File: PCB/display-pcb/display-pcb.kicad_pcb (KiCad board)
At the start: 2 copper layers, 128 x 57 mm, 7 parts, among them J1 B6B-XH-A, J2 B8B-XH-A, SW1 PTS645SL50-2 LFS, SW2 PTS645SL50-2 LFS, SW3 PTS645SL50-2 LFS, SW4 PTS645SL50-2 LFS, U1 NHD-C12864A1Z

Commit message: changes to display and tube pcb
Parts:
- J1, J2: moved to B.Cu
- moved J2 35.7 mm to (122.5, 61.0)
- moved J1 0.25 mm to (122.5, 30.5)
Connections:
- net Net-(U1-SCL) renamed SCL
- net Net-(U1-/RESET) renamed /RESET
- J1 pad 1: Net-(J1-Pad1) -> GND
- J1 pad 2: Net-(J1-Pad2) -> BTN0
- J1 pad 3: Net-(J1-Pad3) -> BTN1
- J1 pad 4: Net-(J1-Pad4) -> BTN2
- J1 pad 5: unconnected-(J1-Pad5) -> BTN3
- J2 pad 2: unconnected-(J2-Pad2) -> GND
- J2 pad 4: Net-(U1-SI) -> GND
- J2 pad 5: Net-(U1-A0) -> SI
- J2 pad 7: Net-(U1-/CS) -> A0
- J2 pad 8: GND -> /CS
- SW1 pad 1: Net-(J1-Pad1) -> BTN0
- SW2 pad 1: Net-(J1-Pad2) -> BTN1
- SW3 pad 1: Net-(J1-Pad3) -> BTN2
- SW4 pad 1: Net-(J1-Pad4) -> BTN3
- U1 pad 3: Net-(U1-SI) -> SI
- U1 pad 5: Net-(U1-A0) -> A0
- U1 pad 7: Net-(U1-/CS) -> /CS
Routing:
- net A0: track 0.00 -> 72.8 mm
- net /CS: track 0.00 -> 68.1 mm
- net SI: track 0.00 -> 60.0 mm
- net 3V3: track 86.1 -> 125.5 mm
- net /RESET: track 31.6 -> 67.0 mm
- net SCL: track 23.2 -> 58.6 mm
- net Net-(U1-/CS): track 33.4 -> 0.00 mm
- net Net-(J1-Pad2): track 31.4 -> 0.00 mm
- net Net-(U1-SI): track 31.3 -> 0.00 mm
- net BTN1: track 0.00 -> 30.5 mm
- net Net-(U1-A0): track 29.8 -> 0.00 mm
- net Net-(J1-Pad4): track 22.6 -> 0.00 mm
- net BTN3: track 0.00 -> 21.6 mm
- net BTN0: track 0.00 -> 19.8 mm
- net Net-(J1-Pad1): track 19.1 -> 0.00 mm
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
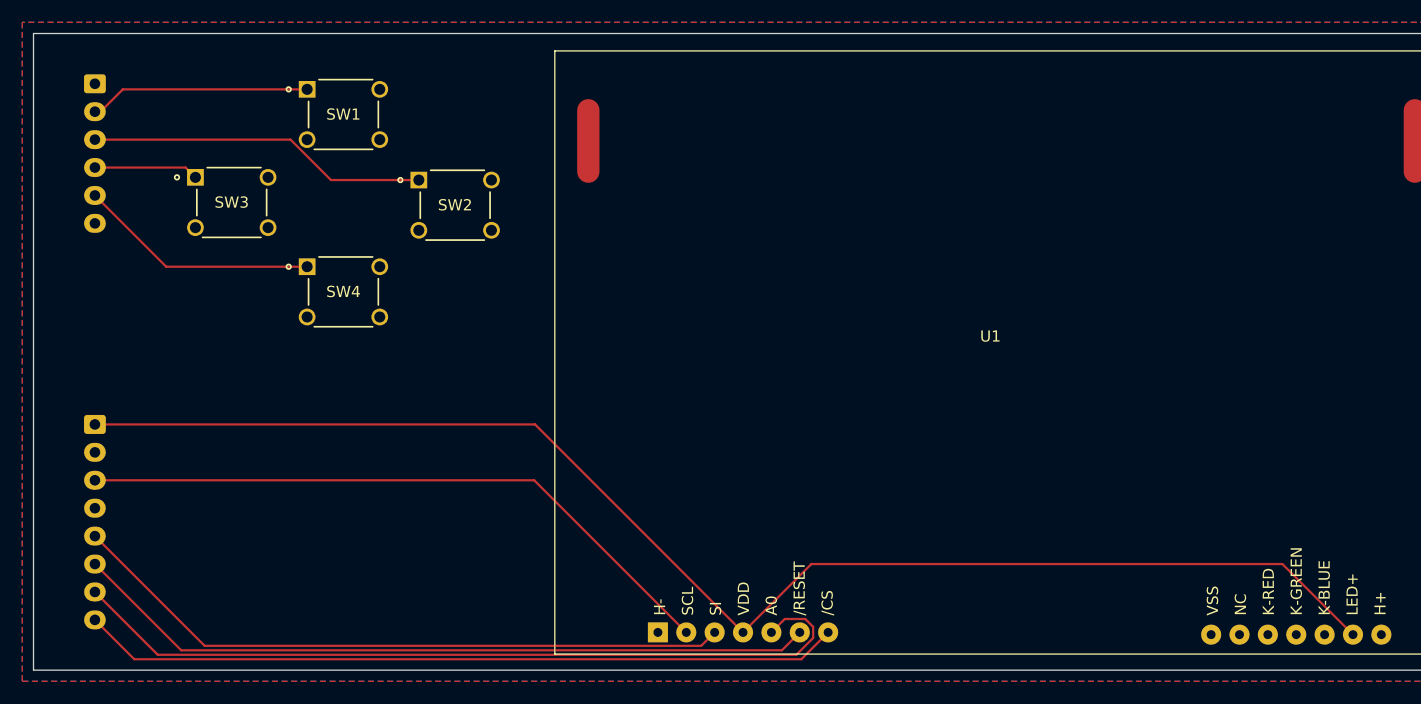
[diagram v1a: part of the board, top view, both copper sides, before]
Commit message: pcb silkscreens mostly
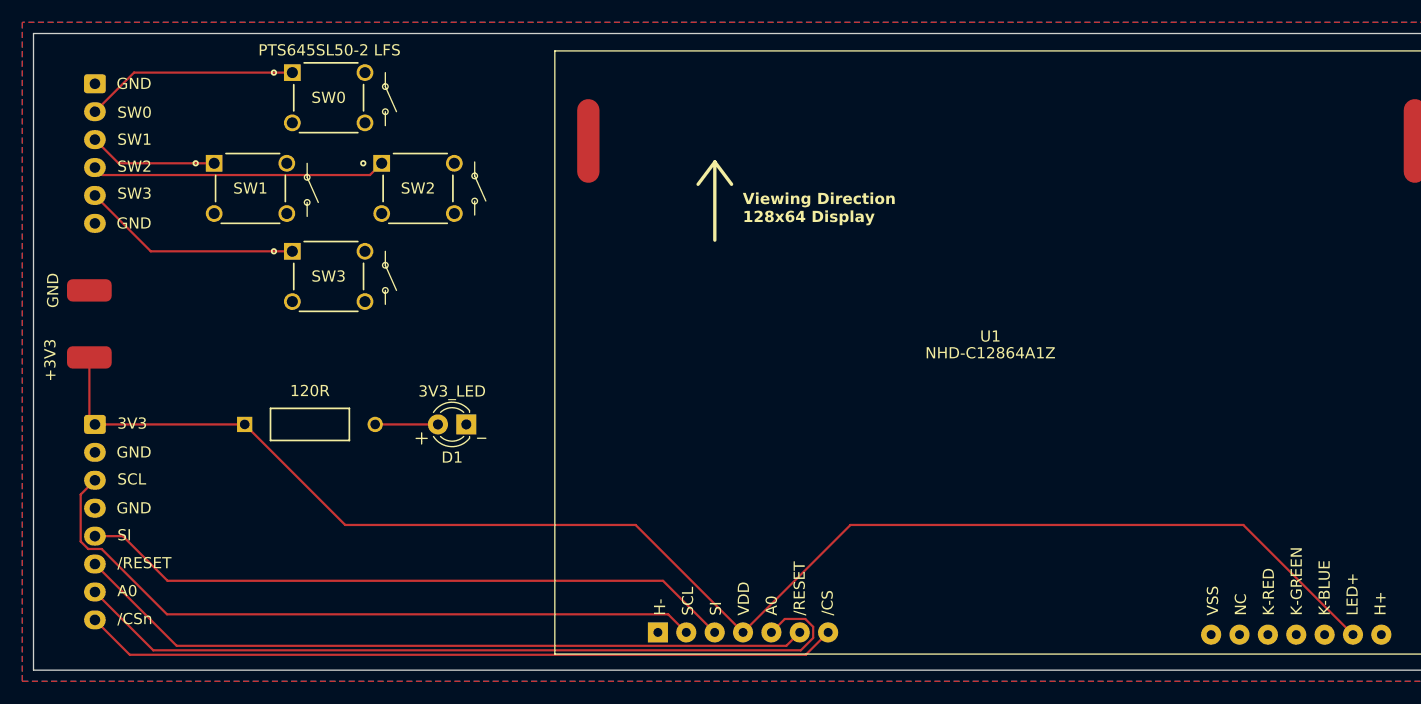
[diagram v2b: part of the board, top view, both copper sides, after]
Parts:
- removed SW4: PTS645SL50-2 LFS, footprints:PTS654S_CNK
- added +3V3: 3V3_Pad, Connector_Wire:SolderWirePad_1x01_SMD_2x4mm, F.Cu at (122.0, 55.0)
- added 120R: 120R, 10k-resistor:YAG_MF25_YAG, F.Cu at (135.9, 61.0)
- added D1: 3V3_LED, LED_THT:LED_D3.0mm, F.Cu at (155.8, 61.0)
- added GND: GND_Pad, Connector_Wire:SolderWirePad_1x01_SMD_2x4mm, F.Cu at (122.0, 49.0)
- added SW0: PTS645SL50-2 LFS, footprints:PTS654S_CNK, F.Cu at (140.2, 29.5)
- moved SW3 10.9 mm to (140.2, 45.5)
- moved SW1 10.6 mm to (133.2, 37.6)
- moved SW2 3.65 mm to (148.2, 37.6)
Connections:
- SW1 pad 1: BTN0 -> BTN1
- SW2 pad 1: BTN1 -> BTN2
- SW3 pad 1: BTN2 -> BTN3
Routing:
- net BTN1: track 30.5 -> 11.6 mm
- net BTN2: track 9.36 -> 26.4 mm
- net 3V3: track 125.5 -> 134.6 mm
- net Net-(D1-A): track 0.00 -> 5.62 mm
- net SCL: track 58.6 -> 63.6 mm
- net BTN3: track 21.6 -> 19.7 mm
- net SI: track 60.0 -> 59.1 mm
- net BTN0: track 19.8 -> 19.1 mm
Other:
- board text added: "/CSn"
- board text added: "/RESET"
- board text added: "3V3"
- board text added: "A0"
- board text added: "GND"
- board text added: "SCL"
- board text added: "SI"
- board text added: "SW0"
- board text added: "SW1"
- board text added: "SW2"
- board text added: "SW3"
- board text added: "Viewing Direction 128x64 Display"

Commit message: pcb stuff i forget
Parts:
- removed +3V3: 3V3_Pad, Connector_Wire:SolderWirePad_1x01_SMD_2x4mm
- removed GND: GND_Pad, Connector_Wire:SolderWirePad_1x01_SMD_2x4mm
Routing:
- net 3V3: track 134.6 -> 129.1 mm
- removed copper zone on F.Cu, net GND
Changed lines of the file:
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@@
 			(outputformat 1)
 			(mirror no)
-			(drillshape 1)
+			(drillshape 0)
 			(scaleselection 1)
-			(outputdirectory "")
+			(outputdirectory "gerber/")
 		)
 	)
@@
 		)
 	)
-	(footprint "Connector_Wire:SolderWirePad_1x01_SMD_2x4mm"
-		(layer "F.Cu")
-		(at 122 49 90)
-		(descr "Wire Pad, Square, SMD Pad,  2mm x 4mm")
-		(tags "MeasurementPoint Square SMDPad 2mmx4mm ")
-		(property "Reference" "GND"
-			(at 0 -3.25 270)
-			(layer "F.SilkS")
-			(effects
-				(font
-					(size 1 1)
-					(thickness 0.15)
-				)
-			)
-		)
-		(property "Value" "GND_Pad"
-			(at 0 2.54 90)
-			(layer "F.Fab")
-			(effects
-				(font
-					(size 1 1)
-					(thickness 0.15)
-				)
-			)
-		)
-		(property "Datasheet" "~"
-			(at 0 0 90)
-			(layer "F.Fab")
-			(hide yes)
-			(effects
-				(font
-					(size 1.27 1.27)
-					(thickness 0.15)
-				)
-			)
-		)
-		(property "Description" "Generic connector, single row, 01x01, script generated"
-			(at 0 0 90)
-			(layer "F.Fab")
-			(hide yes)
-			(effects
-				(font
-					(size 1.27 1.27)
-					(thickness 0.15)
-				)
-			)
-		)
-		(property ki_fp_filters "Connector*:*_1x??_*")
-		(sheetname "/")
-		(sheetfile "display-pcb.kicad_sch")
-		(attr exclude_from_pos_files)
-		(fp_rect
-			(start -1.25 -2.25)
-			(end 1.25 2.25)
-			(stroke
-				(width 0.05)
-				(type solid)
-			)
-			(fill no)
-			(layer "F.CrtYd")
-		)
-		(fp_rect
-			(start -1.15 -2.15)
-			(end 1.15 2.15)
-			(stroke
-				(width 0.1)
-				(type default)
-			)
-			(fill no)
-			(layer "F.Fab")
-		)
-		(fp_text user "${REFERENCE}"
-			(at 0 0 90)
-			(layer "F.Fab")
-			(effects
-				(font
-					(size 1 1)
-					(thickness 0.15)
-				)
-			)
-		)
-		(pad "1" smd roundrect
-			(at 0 0 90)
-			(size 2 4)
-			(layers "F.Cu" "F.Mask")
-			(roundrect_rratio 0.25)
-			(net 4 "GND")
-			(pinfunction "Pin_1")
-			(pintype "passive")
-		)
-		(embedded_fonts no)
-	)
 	(footprint "footprints:PTS654S_CNK"
 		(layer "F.Cu")
@@
 		(embedded_fonts no)
 	)
-	(footprint "Connector_Wire:SolderWirePad_1x01_SMD_2x4mm"
-		(layer "F.Cu")
-		(at 122 55 90)
-		(descr "Wire Pad, Square, SMD Pad,  2mm x 4mm")
-		(tags "MeasurementPoint Square SMDPad 2mmx4mm ")
-		(property "Reference" "+3V3"
-			(at -0.25 -3.5 270)
-			(layer "F.SilkS")
-			(effects
-				(font
-					(size 1 1)
-					(thickness 0.15)
-				)
-			)
-		)
-		(property "Value" "3V3_Pad"
-			(at 0 2.54 90)
-			(layer "F.Fab")
-			(effects
-				(font
-					(size 1 1)
-					(thickness 0.15)
-				)
-			)
-		)
-		(property "Datasheet" "~"
-			(at 0 0 90)
-			(layer "F.Fab")
-			(hide yes)
-			(effects
-				(font
-					(size 1.27 1.27)
-					(thickness 0.15)
-				)
-			)
-		)
-		(property "Description" "Generic connector, single row, 01x01, script generated"
-			(at 0 0 90)
-			(layer "F.Fab")
-			(hide yes)
-			(effects
-				(font
-					(size 1.27 1.27)
-					(thickness 0.15)
-				)
-			)
-		)
-		(property ki_fp_filters "Connector*:*_1x??_*")
-		(sheetname "/")
-		(sheetfile "display-pcb.kicad_sch")
-		(attr exclude_from_pos_files)
-		(fp_rect
-			(start -1.25 -2.25)
-			(end 1.25 2.25)
-			(stroke
-				(width 0.05)
-				(type solid)
-			)
-			(fill no)
-			(layer "F.CrtYd")
-		)
-		(fp_rect
-			(start -1.15 -2.15)
-			(end 1.15 2.15)
-			(stroke
-				(width 0.1)
-				(type default)
-			)
-			(fill no)
-			(layer "F.Fab")
-		)
-		(fp_text user "${REFERENCE}"
-			(at 0 0 90)
-			(layer "F.Fab")
-			(effects
-				(font
-					(size 1 1)
-					(thickness 0.15)
-				)
-			)
-		)
-		(pad "1" smd roundrect
-			(at 0 0 90)
-			(size 2 4)
-			(layers "F.Cu" "F.Mask")
-			(roundrect_rratio 0.25)
-			(net 8 "3V3")
-			(pinfunction "Pin_1")
-			(pintype "passive")
-		)
-		(embedded_fonts no)
-	)
 	(footprint "footprints:PTS654S_CNK"
 		(layer "F.Cu")
@@
 	)
 	(segment
-		(start 122 55)
-		(end 122 60.5)
-		(width 0.2)
-		(layer "F.Cu")
-		(net 8)
-	)
-	(segment
 		(start 180.52425 79.61995)
 		(end 190.1442 70)
@@
 		(net_name "GND")
 		(locked yes)
-		(layers "F.Cu" "B.Cu")
+		(layer "B.Cu")
 		(hatch edge 0.5)
+		(priority 1)
 		(connect_pads
 			(clearance 0.5)
@@
 		(polygon
 			(pts
-				(xy 116 25) (xy 116 84) (xy 246 84) (xy 246 25)
+				(xy 106 15) (xy 105.5 97) (xy 261 97) (xy 259.5 14)
 			)
 		)

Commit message: PCB updates
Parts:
- removed SW0: PTS645SL50-2 LFS, footprints:PTS654S_CNK
- added J3: B8B-XH-A, Connector_JST:JST_XH_B8B-XH-A_1x08_P2.50mm_Vertical, B.Cu at (125.5, 121.5)
- added SW4: PTS645SL50-2 LFS, footprints:PTS654S_CNK, F.Cu at (140.7, 73.6)
- added U2: ~, microsd:pmod-microsd, F.Cu at (140.1, 114.5)
- moved J2 68.7 mm to (155.5, 121.2), turned to 90 degrees
- moved J1 56.6 mm to (125.5, 87.0), turned to 90 degrees
- moved SW1 52.5 mm to (140.7, 89.6)
- moved D1 47.0 mm to (126.8, 98.0)
- moved SW2 46.5 mm to (133.2, 81.6)
- moved U1 43.2 mm to (198.7, 96.6)
- moved SW3 37.1 mm to (148.7, 81.6)
- moved R1 31.5 mm to (134.5, 92.5), turned to 180 degrees
- renumbered 120R to R1
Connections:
- J2 pad 6: /RESET -> A0
- J2 pad 7: A0 -> /RESET
- SW1 pad 1: BTN1 -> BTN0
- SW2 pad 1: BTN2 -> BTN1
- SW3 pad 1: BTN3 -> BTN2
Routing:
- net SCL: track 63.6 -> 18.6 mm
- net A0: track 72.5 -> 29.3 mm
- net SI: track 59.1 -> 23.2 mm
- net /RESET: track 66.6 -> 32.9 mm
- net /CS: track 67.8 -> 36.4 mm
- net SD_CSn: track 0.00 -> 27.3 mm
- net SD_MOSI: track 0.00 -> 22.7 mm
- net SD_MISO: track 0.00 -> 19.1 mm
- net SD_SCK: track 0.00 -> 14.5 mm
- net SD_3V3: track 0.00 -> 8.60 mm
- net 3V3: track 129.1 -> 120.5 mm
- net BTN1: track 11.6 -> 7.83 mm
- net BTN3: track 19.7 -> 16.6 mm
- net BTN2: track 26.4 -> 24.1 mm
- net BTN0: track 19.1 -> 17.3 mm
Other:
- board size 128 x 57 mm -> 120.5 x 57 mm
- board text added: "/CS"
- board text added: "/RST"
- board text added: "BTN0"
- board text added: "BTN1"
- board text added: "BTN2"
- board text added: "BTN3"
- board text added: "CSn"
- board text added: "MISO"
- board text added: "MOSI"
- board text added: "SCK"
- board text removed: "/CSn"
- board text removed: "/RESET"
- board text removed: "SCL"
- board text removed: "SI"
- board text removed: "SW0"
- board text removed: "SW1"
- board text removed: "SW2"
- board text removed: "SW3"
